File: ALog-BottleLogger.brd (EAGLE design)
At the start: 120.7 x 44.5 mm, 102 parts, among them IC2 ATMEGA644M, J6 5.5x2.1mm Barrel, Q1 220mA/50V/3.5Ω, Q4 4.3A/20V/54mΩ, Q5 4.3A/20V/54mΩ, Q6 4.3A/20V/54mΩ, Q7 4.3A/20V/54mΩ, Q8 220mA/50V/3.5Ω, Q9 220mA/50V/3.5Ω, U2 FT231X-Q

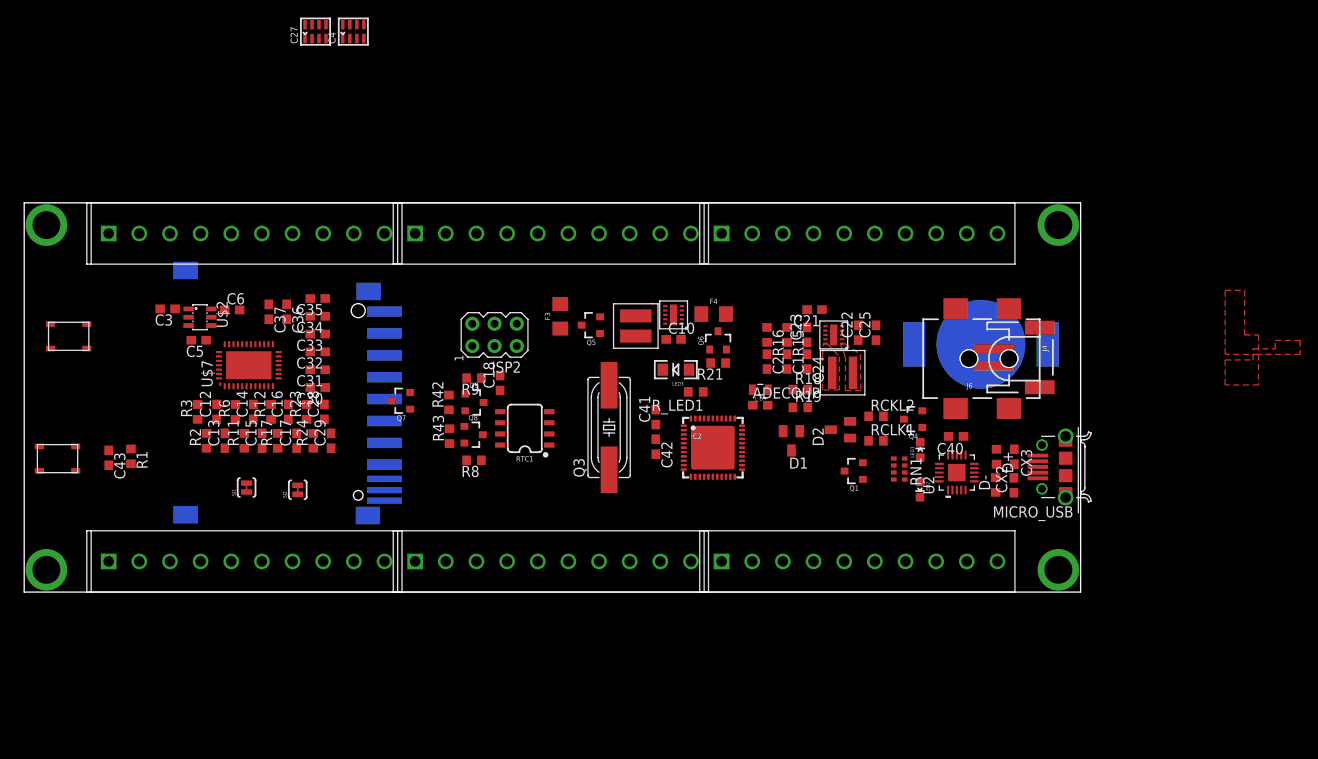
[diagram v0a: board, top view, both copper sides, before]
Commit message: 4.75 inches long, reference voltages broken out
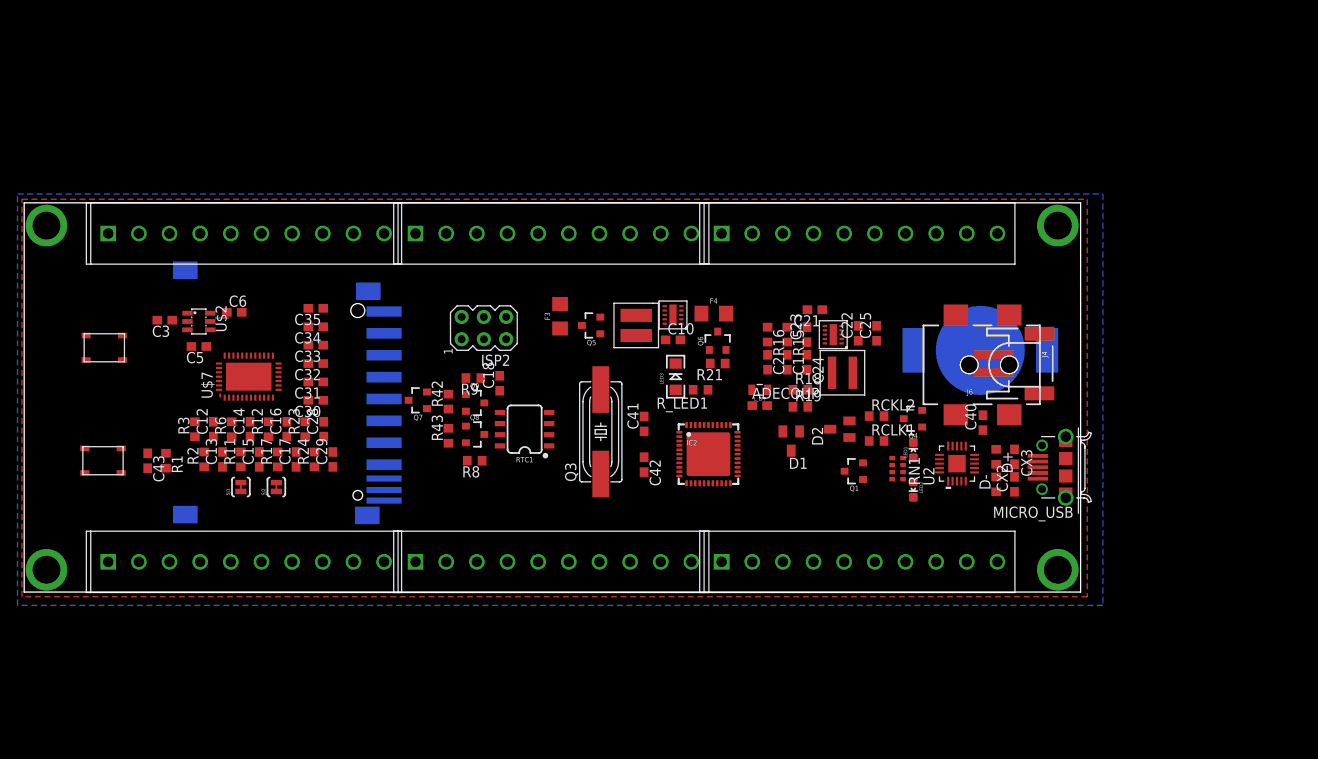
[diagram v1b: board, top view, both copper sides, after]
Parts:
- removed C27, C4: 10nF, rc-master-smd:CECJ-CTS-031817
- removed C36, C37: 10nF, rcl:C0603
- moved U$4 5.20 mm to (9.00, 15.0)
- moved C43 4.46 mm to (14.1, 15.0)
- moved S1 4.28 mm to (9.15, 27.9)
- moved R1 4.04 mm to (16.2, 15.0)
- moved C40 3.45 mm to (109.5, 19.4), turned to 90 degrees
- moved SJ2 2.46 mm to (28.8, 12.0)
- moved C42 2.45 mm to (70.8, 14.6)
- moved R11 2.16 mm to (24.8, 15.2)
- moved C15 2.15 mm to (26.9, 15.2)
- moved R2 2.14 mm to (20.6, 15.2)
- moved C13 2.14 mm to (22.6, 15.2)
- moved C29 2.13 mm to (35.2, 15.2)
- moved R24 2.13 mm to (33.1, 15.2)
- moved C17 2.12 mm to (31.1, 15.2)
- moved R17 2.12 mm to (28.9, 15.2)
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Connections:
- net D12 renamed D12~
- net D13 renamed D13~
- net D14 renamed D14~
- net D15 renamed D15~
- removed net ADC14: C36.2, J14.P$2
- removed net ADC15: C37.2, J14.P$1
- removed net D19: IC2.22
- removed net D3: IC2.43
- removed net GND2: C4.B2, C4.D2
- removed net GND4: C27.A2, C27.B2, C27.C2, C27.D2
- removed net N$14: C4.C2
- removed net REF_EN: U$2.3
- removed net SD-VCC_CTRL: IC2.21
- removed net SS: J2.P$4
- new net 1.8V_EN: IC2.22, U$2.3
- net +3V3: now also J14.P$2
- net 1.8V_REF: now also J14.P$1
- net D1: no longer J2.P$9
- net D3~: now also IC2.43
- net GND: no longer C36.1, C37.1
- net MCU_ADC0: now also J2.P$9
- net MISO: no longer J2.P$2
- net MISO/D6: now also J2.P$2
- net MOSI: no longer J2.P$3
- net MOSI/D5: now also J2.P$3
- net SCK: no longer J2.P$1
- net SCK/D7: now also J2.P$1
- net SD_VCC_CTRL: now also IC2.21
- net SS/D4: now also J2.P$4
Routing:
- added copper zone on layer 16, net GND
- removed copper zone on layer 1, net 3.3V
- removed copper zone on layer 1, net 5V
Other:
- board text added: "1.8V_REF"
- board text added: "3V3_REF"
- board text added: "ADC0"
- board text removed: "A14"
- board text removed: "A15"
- board text removed: "D1"
- board text removed: "ISP"
- board text removed: "RX"
- board text removed: "TX"

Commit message: fully routed, looking for review
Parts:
- moved CLOCK_BATT 22.8 mm to (94.0, 10.5), turned to 180 degrees
- moved S1 14.0 mm to (10.7, 13.9), turned to 270 degrees
- moved U$4 13.9 mm to (10.7, 28.8), turned to 90 degrees
- moved C43 12.8 mm to (14.1, 27.8)
- moved R1 12.8 mm to (16.2, 27.8)
- moved J4 4.87 mm to (117.2, 22.1)
- moved R_LED1 4.65 mm to (72.6, 23.2)
- moved F4 3.90 mm to (82.3, 30.3), turned to 90 degrees
- moved F3 2.70 mm to (63.9, 31.5), turned to 180 degrees
- moved Q5 2.33 mm to (65.4, 28.2)
- moved MICRO_USB 2.12 mm to (119.2, 12.2)
- moved LED3 1.38 mm to (73.3, 25.5), turned to 0 degrees
- moved D1 1.24 mm to (87.3, 16.1)
- moved C12 0.90 mm to (20.7, 18.6)
- moved R2 0.90 mm to (19.6, 15.2)
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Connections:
- net +3V3: no longer J14.P$2
- net 1.8V_REF: no longer J14.P$1
- net ADC10: now also J14.P$10; no longer J15.P$2
- net ADC11: now also J14.P$9; no longer J15.P$1
- net ADC12: now also J14.P$5; no longer J14.P$7
- net ADC13: now also J14.P$4; no longer J14.P$6
- net ADC8: now also J15.P$5; no longer J15.P$7
- net ADC9: now also J15.P$4; no longer J15.P$6
- net BATT+: now also J2.P$9
- net D15~: now also J2.P$8; no longer J2.P$10
- net D3~: now also J2.P$6; no longer J2.P$8
- net EXT_3.3V: now also J14.P$2, J14.P$7, J15.P$2, J15.P$7, J2.P$4; no longer J14.P$4, J14.P$9, J15.P$4, J15.P$9, J2.P$6
- net EXT_5V: now also J14.P$8, J15.P$8, J2.P$5; no longer J14.P$10, J15.P$10, J2.P$7
- net EXT_5V1: now also J14.P$3, J15.P$3; no longer J14.P$5, J15.P$5
- net GND: now also J14.P$1, J14.P$6, J15.P$1, J15.P$6, J2.P$10, J2.P$3; no longer J14.P$3, J14.P$8, J15.P$3, J15.P$8, J2.P$5
- net MCU_ADC0: now also J2.P$7; no longer J2.P$9
- net MISO/D6: now also J15.P$10; no longer J2.P$2
- net MOSI/D5: now also J2.P$1; no longer J2.P$3
- net SCK/D7: now also J15.P$9; no longer J2.P$1
- net SS/D4: now also J2.P$2; no longer J2.P$4
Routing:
- net EXT_3.3V: track 0.00 -> 211.8 mm
- net EXT_5V: track 0.00 -> 203.2 mm
- net +3V3: track 0.00 -> 195.7 mm, vias 0 -> 11
- net +5V: track 0.00 -> 149.8 mm, vias 0 -> 6
- net EXT_5V1: track 0.00 -> 117.4 mm
- net RTC_INT: track 0.00 -> 104.2 mm, vias 0 -> 4
- net SDA_HV: track 0.00 -> 95.7 mm, vias 0 -> 7
- net N$39: track 0.00 -> 91.1 mm, vias 0 -> 4
- net 1.8V_EN: track 0.00 -> 90.6 mm, vias 0 -> 2
- net RST: track 0.00 -> 86.9 mm, vias 0 -> 2
- net 1.8V_REF: track 0.00 -> 77.7 mm, vias 0 -> 2
- net SCL: track 0.00 -> 76.7 mm, vias 0 -> 4
- net SDA: track 0.00 -> 75.2 mm, vias 0 -> 5
- net ADC7: track 0.00 -> 60.0 mm, vias 0 -> 4
- net MISO/D6: track 0.00 -> 59.5 mm, vias 0 -> 3
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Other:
- board text added: "BATT"
- board text removed: "1.8V_REF"
- board text removed: "3V3_REF"

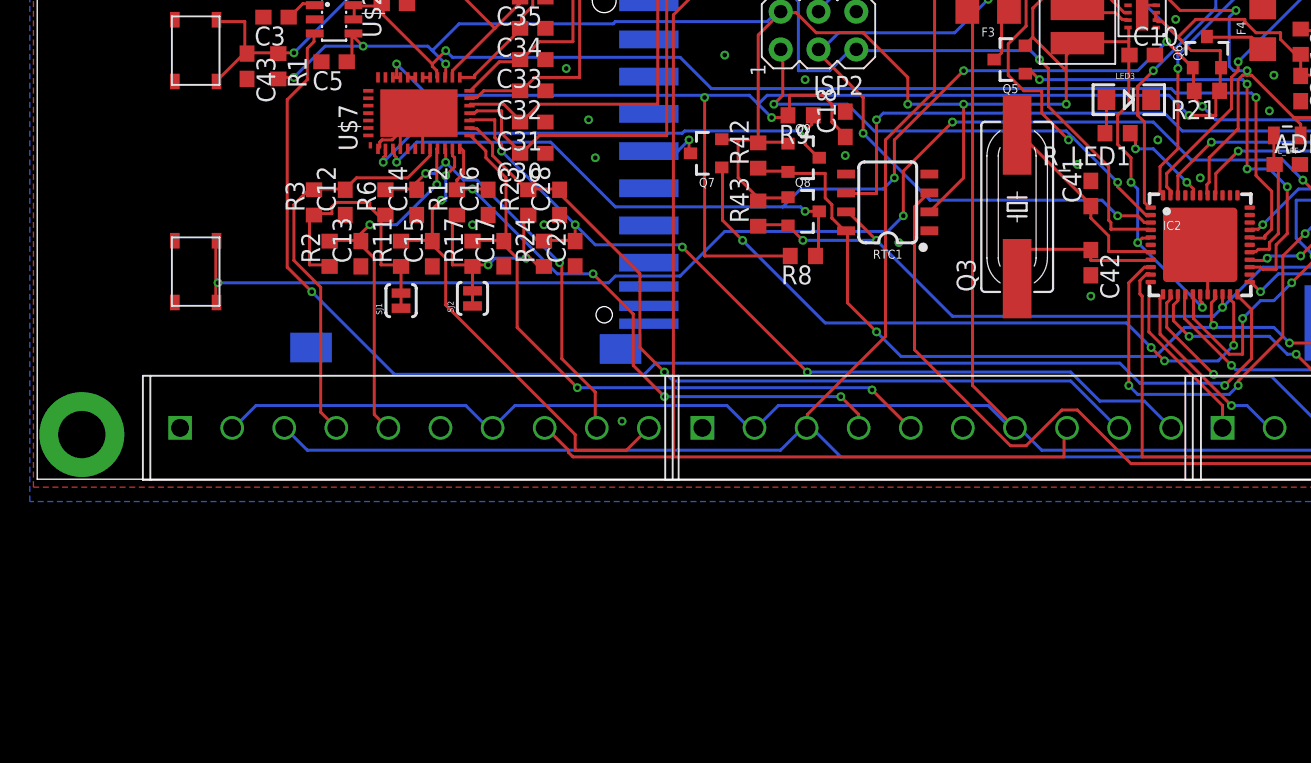
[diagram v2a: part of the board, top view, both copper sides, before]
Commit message: Add 10K pull downs on mosphets for external controls
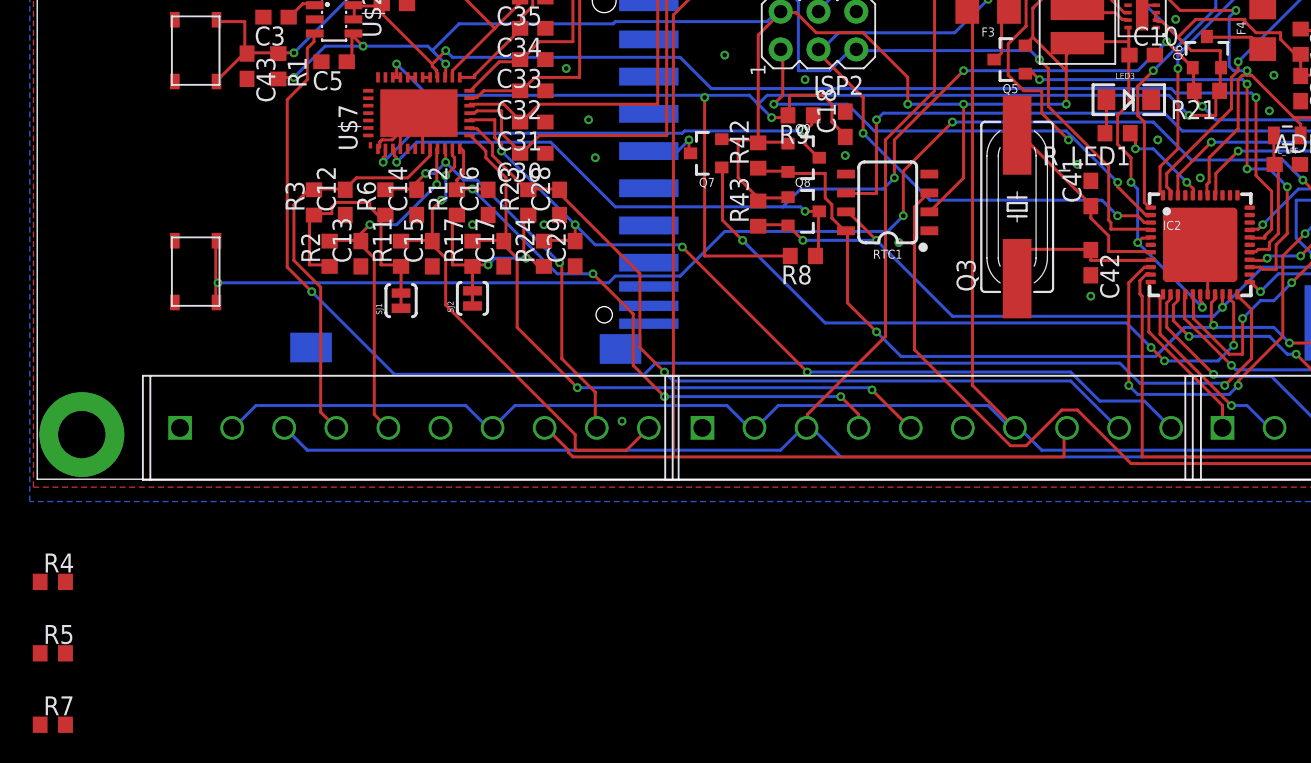
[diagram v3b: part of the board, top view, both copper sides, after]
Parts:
- added R4, R5, R7: 10k, rcl:R0603@1
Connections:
- net +3V3: now also R21.2
- net +5V: no longer R21.1
- net 3.3V_EXT_CTRL: now also R5.2
- net 5V_EXT_CTRL: now also R21.1
- net GND: now also R7.2
- net SDA_HV: now also R7.1; no longer R21.2
- net SD_VCC_CTRL: now also R4.2

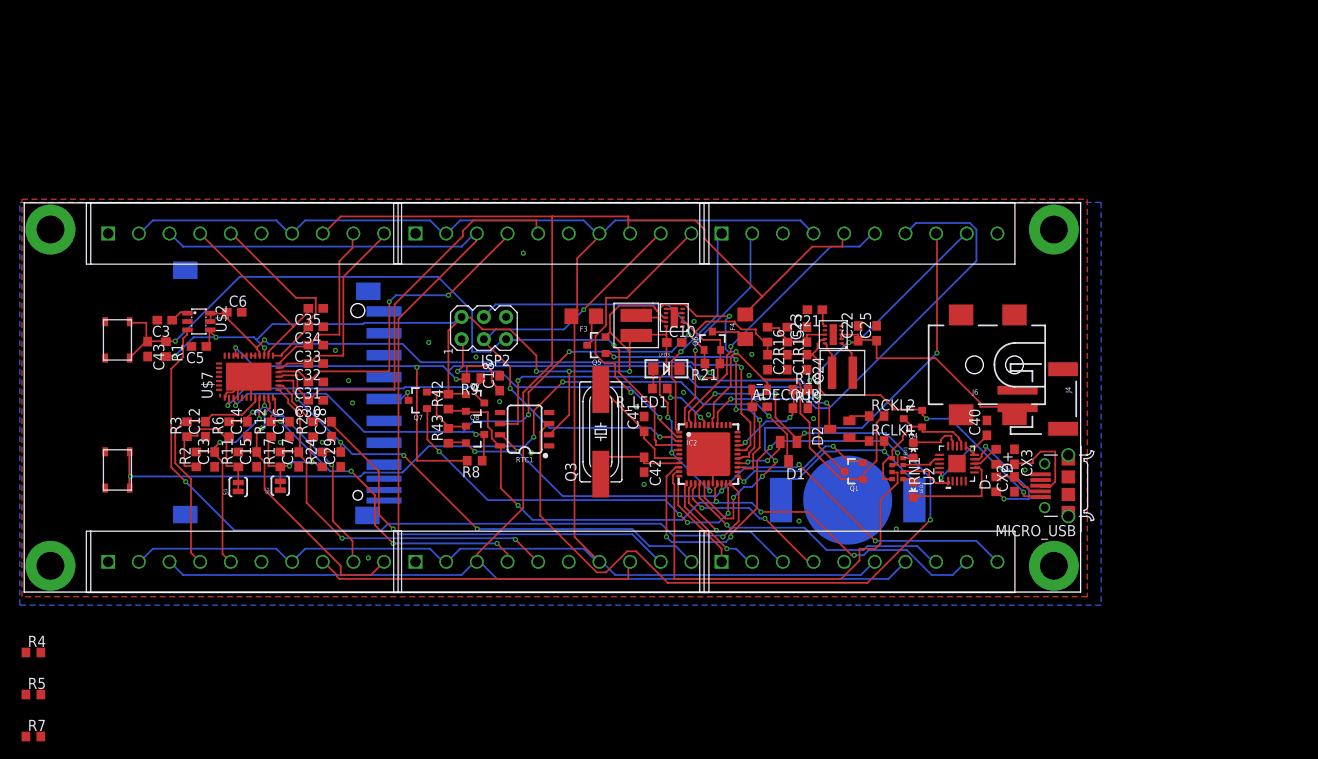
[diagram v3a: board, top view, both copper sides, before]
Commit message: Fixed 5V control and a few other things, fully routed and ready for review
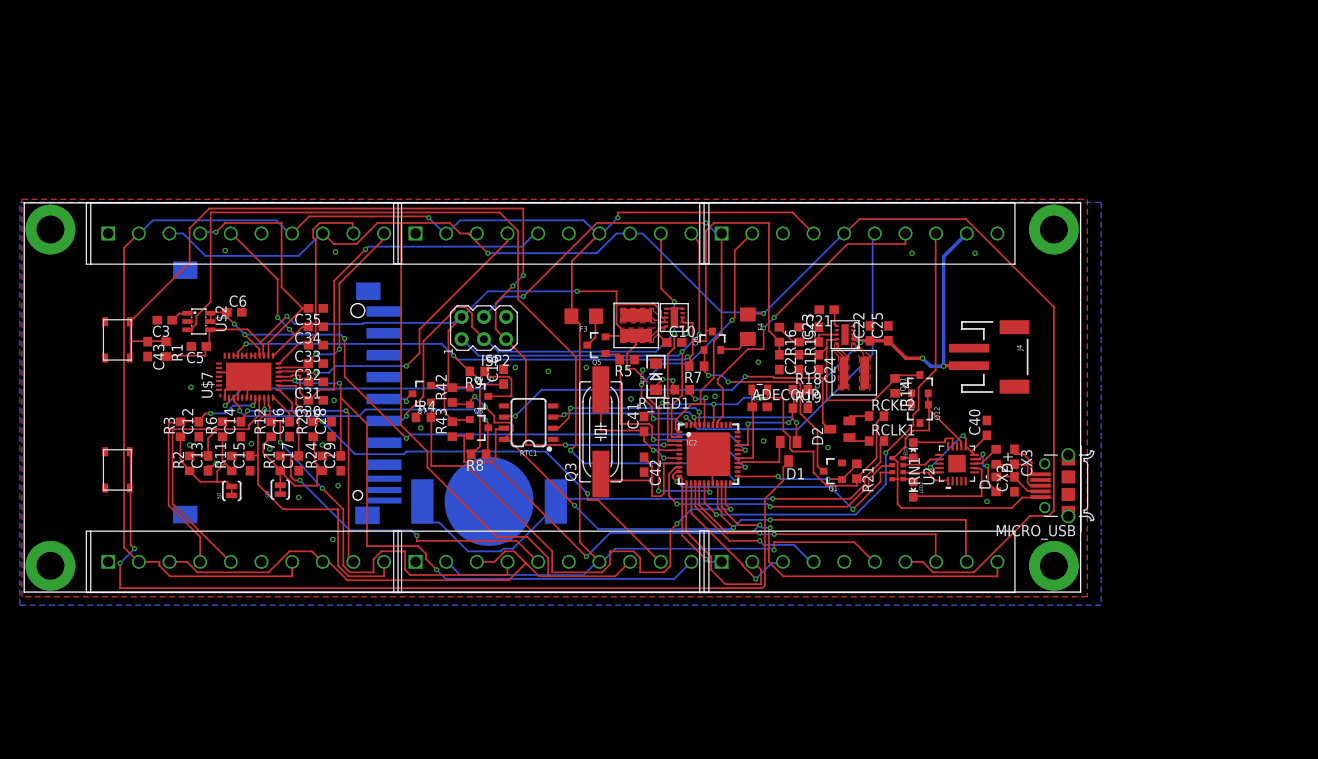
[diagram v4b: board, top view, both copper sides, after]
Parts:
- removed J6: 5.5x2.1mm Barrel, SparkFun-Connectors:POWER_JACK_SMD
- removed Q4: 4.3A/20V/54mΩ, SparkFun-DiscreteSemi:SOT23-3
- added Q11: 220mA/50V/3.5Ω, SparkFun-DiscreteSemi:SOT23-3
- added Q12: 4.3A/20V/54mΩ, SparkFun-DiscreteSemi:SOT23-3
- added R14: 10k, rcl:R0603@1
- moved R7 86.8 mm to (76.8, 25.8), turned to 180 degrees
- moved R5 77.8 mm to (68.8, 26.6), turned to 180 degrees
- moved R4 52.0 mm to (45.6, 19.9)
- moved CLOCK_BATT 41.0 mm to (53.1, 10.3)
- moved R21 20.6 mm to (95.1, 13.8), turned to 270 degrees
- moved J4 7.34 mm to (111.6, 26.9)
- moved R_LED1 2.55 mm to (75.2, 23.1)
- moved Q1 2.40 mm to (92.4, 13.8)
- moved LED3 1.50 mm to (72.2, 24.6), turned to 90 degrees
- moved C21 1.35 mm to (91.7, 32.2)
- moved C25 1.35 mm to (98.7, 29.6)
- moved C1 1.35 mm to (88.5, 26.2)
- moved C2 1.35 mm to (86.2, 26.2)
- moved C22 1.35 mm to (96.6, 29.6)
- moved C23 1.35 mm to (90.8, 29.4)
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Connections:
- net MISO renamed MISO/D5
- net MOSI renamed MOSI/D6
- removed net D1: IC2.41
- removed net EXT_5V1: J14.P$3, J15.P$3, J16.P$8, J8.P$8
- removed net N$23: F4.1, Q6.3
- removed net SCK: SD.5
- new net N$11: Q11.1, Q12.2, R14.2
- new net N$14: F4.2, Q6.2
- new net N$6: Q1.3, Q6.1, R7.1
- new net RTC_EN: IC2.41, RTC1.2
- net +3V3: no longer Q1.1, RTC1.2
- net +5V: now also Q11.3, Q6.3, R14.1, R7.2; no longer MICRO_USB.1, Q4.2, Q6.2
- net 5V_EXT_CTRL: now also Q1.1; no longer Q1.2
- net BATT+: no longer J6.VIN0
- net EXT_5V: now also F4.1, J14.P$3, J15.P$3, J16.P$8, J8.P$8; no longer F4.2
- net GND: now also Q1.2, Q12.3, R4.1, R5.1; no longer J6.GND, J6.P$4, R7.2
- net SCK/D7: now also SD.5
- net SDA_HV: no longer Q1.3, Q6.1, R7.1
- net VUSB: now also MICRO_USB.1, Q11.2, Q12.1; no longer Q4.1, Q4.3
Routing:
- net EXT_5V1: track 117.4 -> 0.00 mm
- net EXT_5V: track 203.2 -> 279.6 mm, vias 0 -> 2
- net RTC_INT: track 104.2 -> 31.8 mm, vias 4 -> 3
- net SDA_HV: track 95.5 -> 35.1 mm, vias 7 -> 2
- net RTC_BATT: track 23.9 -> 65.1 mm
- net N$6: track 0.00 -> 25.1 mm, vias 0 -> 2
- net EXT_3.3V: track 211.8 -> 235.5 mm, vias 0 -> 3
- net +3V3: track 195.7 -> 172.1 mm, vias 11 -> 7
- net VUSB: track 17.2 -> 39.2 mm
- net RST: track 86.9 -> 108.2 mm, vias 2 -> 4
- net RTC_EN: track 0.00 -> 19.8 mm, vias 0 -> 2
- net SCK/D7: track 53.9 -> 72.6 mm
- net TX_USB: track 48.4 -> 30.1 mm, vias 0 -> 2
- net SDA: track 75.2 -> 91.5 mm, vias 5 -> 3
- net ADC7: track 60.0 -> 75.6 mm, vias 4 -> 3
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- added copper zone on layer 1, net +3V3
- added copper zone on layer 1, net N$1
- added copper zone on layer 1, net N$19
- added copper zone on layer 1, net N$20
